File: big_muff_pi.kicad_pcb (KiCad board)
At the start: 2 copper layers, 56.3 x 18 mm, 54 parts, among them Q1 BC817, Q2 BC817, Q3 BC817, Q5 BC817

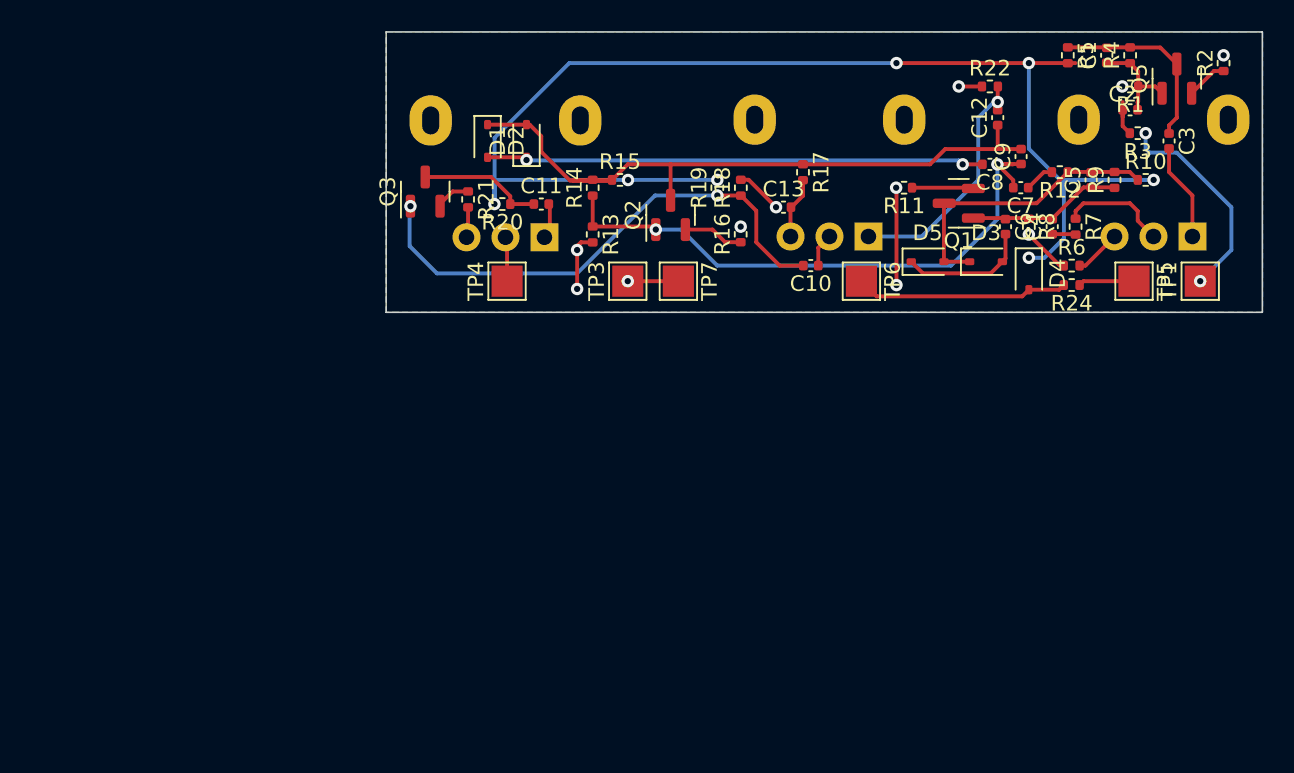
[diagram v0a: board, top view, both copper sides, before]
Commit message: Moved to 0603, all basic parts. Placement done.
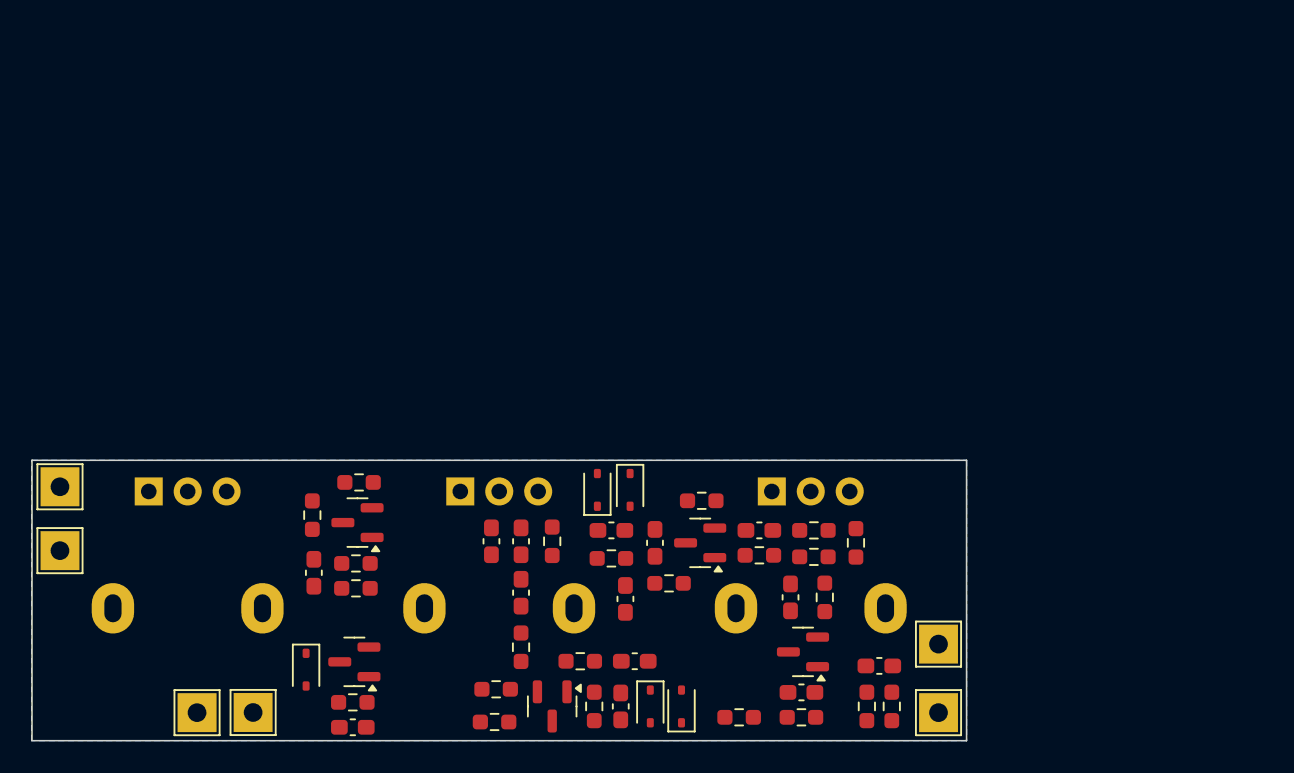
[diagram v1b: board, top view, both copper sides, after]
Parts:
- removed TP3: gnd, TestPoint:TestPoint_Pad_2.0x2.0mm
- removed TP5: Red Error LED, TestPoint:TestPoint_Pad_2.0x2.0mm
- removed TP6: Power Supply, TestPoint:TestPoint_Pad_2.0x2.0mm
- removed TP7: ground, TestPoint:TestPoint_Pad_2.0x2.0mm
- added C14: 10u, Capacitor_SMD:C_0603_1608Metric_Pad1.08x0.95mm_HandSolder, F.Cu at (120.6, 117.1)
- added Q4: MMBT5551, Package_TO_SOT_SMD:SOT-23, F.Cu at (149.5, 112.3)
- added TP11: input, TestPoint:TestPoint_THTPad_2.5x2.5mm_Drill1.2mm, F.Cu at (114.2, 116.2)
- added TP12: ground, TestPoint:TestPoint_THTPad_2.5x2.5mm_Drill1.2mm, F.Cu at (101.8, 105.8)
- added TP13: ground, TestPoint:TestPoint_THTPad_2.5x2.5mm_Drill1.2mm, F.Cu at (158.2, 111.8)
- added TP14: ground, TestPoint:TestPoint_THTPad_2.5x2.5mm_Drill1.2mm, F.Cu at (110.6, 116.2)
- C1, C10, C11, C13, C2, C3, C4, C5, C6, C7, C8, C9: footprint Capacitor_SMD:C_0402_1005Metric -> Capacitor_SMD:C_0603_1608Metric_Pad1.08x0.95mm_HandSolder
- C12: value 4n -> 4.7n; footprint Capacitor_SMD:C_0402_1005Metric -> Capacitor_SMD:C_0603_1608Metric_Pad1.08x0.95mm_HandSolder
- Q1, Q2, Q3, Q5: value BC817 -> MMBT5551
- R1, R10, R11, R12, R13, R14, R15, R16, R17, R18, R19, R2, R20, R21, R22, R3, R4, R5, R6, R7, R8, R9: footprint Resistor_SMD:R_0402_1005Metric -> Resistor_SMD:R_0603_1608Metric_Pad0.98x0.95mm_HandSolder
- R24: value 510 -> 1k; footprint Resistor_SMD:R_0402_1005Metric -> Resistor_SMD:R_0603_1608Metric_Pad0.98x0.95mm_HandSolder
- RV1: value 10k -> 100k
- TP1, TP4: footprint TestPoint:TestPoint_Pad_2.0x2.0mm -> TestPoint:TestPoint_THTPad_2.5x2.5mm_Drill1.2mm
- moved Q5 64.7 mm to (120.7, 112.9), turned to 180 degrees
- moved R24 53.4 mm to (120.6, 115.5)
- moved D4 52.9 mm to (117.6, 113.4)
- moved R4 47.4 mm to (149.4, 116.5), turned to 180 degrees
- moved R5 47.4 mm to (145.4, 116.5), turned to 0 degrees
- moved R22 46.9 mm to (131.4, 112.0), turned to 90 degrees
- moved C1 45.4 mm to (149.4, 114.9), turned to 180 degrees
- moved C9 43.7 mm to (137.8, 115.8), turned to -90 degrees
- moved R1 43.2 mm to (153.6, 115.8), turned to -90 degrees
- moved C12 43.2 mm to (131.4, 108.5), turned to -90 degrees
- moved R2 42.8 mm to (150.9, 108.8), turned to -90 degrees
- moved R3 40.0 mm to (155.2, 115.8), turned to 90 degrees
- moved C8 39.2 mm to (138.7, 112.9), turned to 0 degrees
- moved C2 39.2 mm to (154.4, 113.2), turned to 180 degrees
- moved D2 38.4 mm to (141.7, 115.8), turned to 90 degrees
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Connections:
- C1 pad 1: Net-(Q5-B) -> Net-(Q4-B)
- C1 pad 2: Net-(Q5-C) -> Net-(Q4-C)
- C2 pad 2: Net-(Q5-B) -> Net-(Q4-B)
- C3 pad 1: Net-(Q5-C) -> Net-(Q4-C)
- D4 pad 1: 9V -> Net-(D4-K)
- Q5 pad 2: Net-(Q5-E) -> 9V
- Q5 pad 3: Net-(Q5-C) -> Net-(D4-K)
- R1 pad 1: Net-(Q5-B) -> Net-(Q4-B)
- R10 pad 1: Net-(D3-K) -> 9V
- R10 pad 2: 9V -> Net-(D3-K)
- R15 pad 1: Net-(D1-A) -> 9V
- R15 pad 2: 9V -> Net-(D1-A)
- R2 pad 1: Net-(Q5-E) -> 0
- R2 pad 2: 0 -> Net-(Q4-E)
- R24 pad 1: Net-(R24-Pad1) -> Net-(Q5-B)
- R24 pad 2: Net-(D4-A) -> Net-(D4-K)
- R4 pad 1: Net-(Q5-B) -> Net-(Q4-B)
- R4 pad 2: Net-(Q5-C) -> Net-(Q4-C)
- R5 pad 1: Net-(Q5-C) -> 9V
- R5 pad 2: 9V -> Net-(Q4-C)
- R6 pad 1: 0 -> Net-(R6-Pad1)
- R6 pad 2: Net-(R6-Pad2) -> 0
- RV1 pad 3: Net-(R6-Pad2) -> Net-(R6-Pad1)
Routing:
- net 9V: track 86.0 -> 0.00 mm, vias 7 -> 0
- net Net-(D1-A): track 43.8 -> 0.00 mm
- net Net-(Q2-B): track 38.2 -> 0.00 mm, vias 2 -> 0
- net Net-(Q3-B): track 33.7 -> 0.00 mm, vias 2 -> 0
- net Net-(D1-K): track 32.0 -> 0.00 mm, vias 2 -> 0
- net 0: track 23.0 -> 0.00 mm, vias 11 -> 0
- net Net-(D3-K): track 18.9 -> 0.00 mm
- net Net-(C12-Pad2): track 15.7 -> 0.00 mm, vias 1 -> 0
- net Net-(D4-A): track 13.7 -> 0.00 mm
- net Net-(R3-Pad1): track 13.6 -> 0.00 mm, vias 2 -> 0
- net Net-(Q5-C): track 12.1 -> 0.00 mm
- net Net-(Q1-B): track 9.89 -> 0.00 mm
- net Net-(D3-A): track 8.32 -> 0.00 mm
- net Net-(Q3-C): track 7.98 -> 0.00 mm
- net Net-(R7-Pad1): track 6.95 -> 0.00 mm
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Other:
- board size 56.3 x 18 mm -> 60 x 18 mm

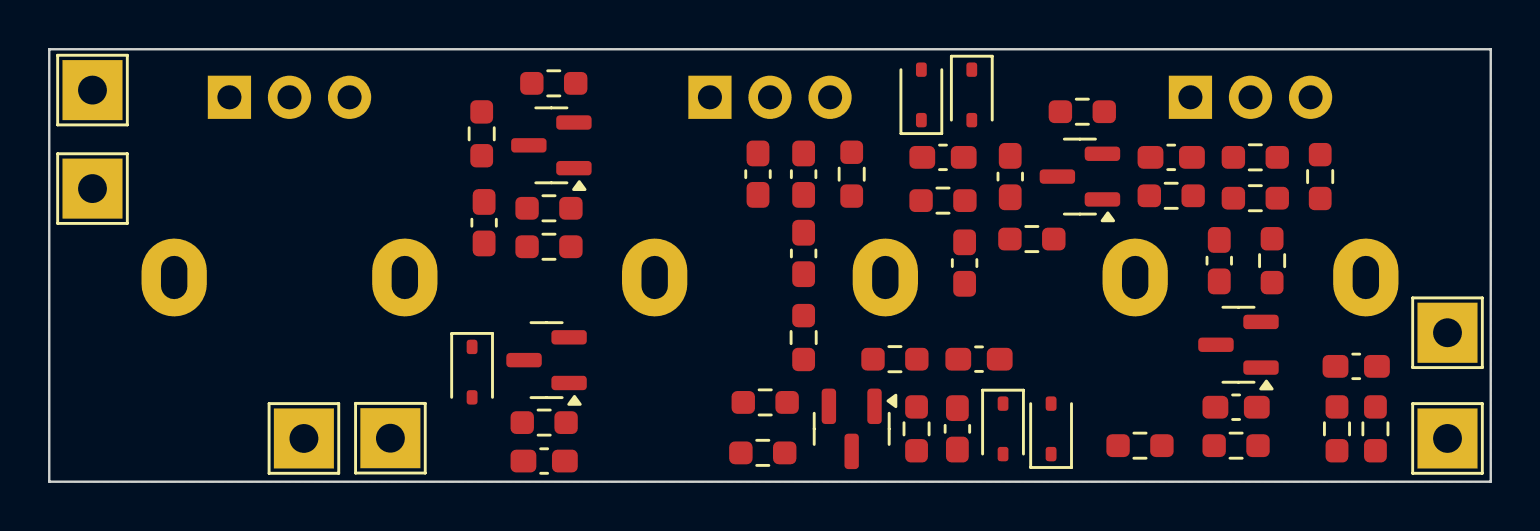
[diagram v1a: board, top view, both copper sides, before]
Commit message: Added capacitance, switches.
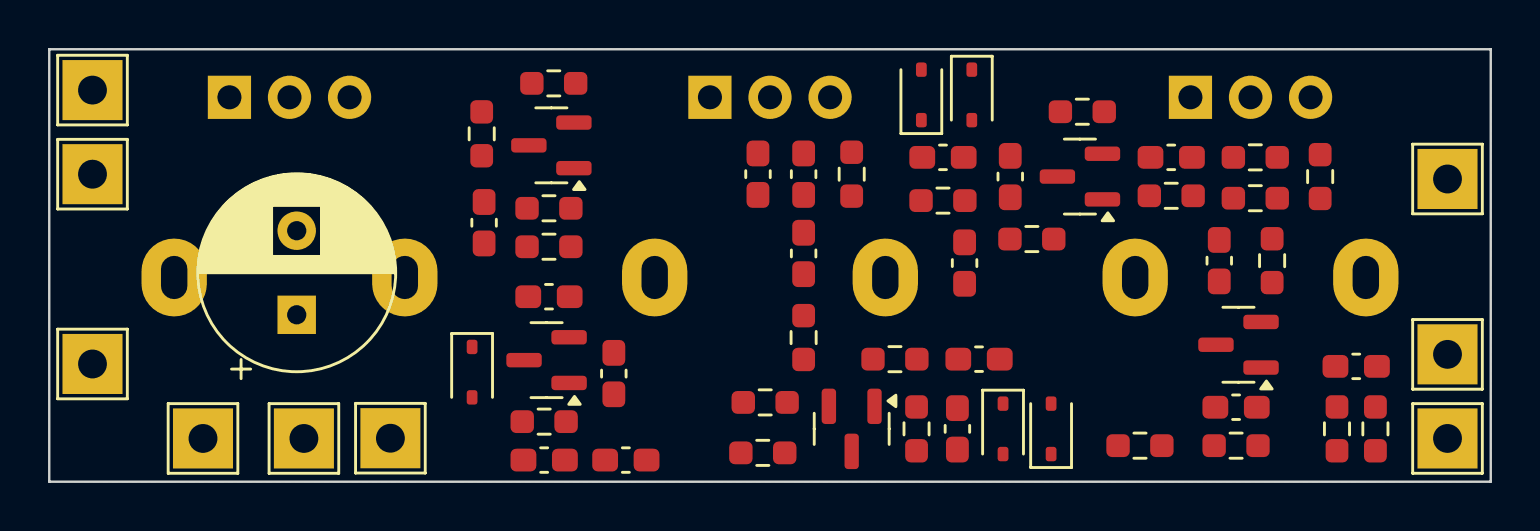
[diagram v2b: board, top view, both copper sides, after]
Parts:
- added C16: 10u, Capacitor_SMD:C_0603_1608Metric_Pad1.08x0.95mm_HandSolder, F.Cu at (120.8, 110.3)
- added C17: 10u, Capacitor_SMD:C_0603_1608Metric_Pad1.08x0.95mm_HandSolder, F.Cu at (123.5, 113.5)
- added C18: 100n, Capacitor_SMD:C_0603_1608Metric_Pad1.08x0.95mm_HandSolder, F.Cu at (124.0, 117.1)
- added C19: 470u, Capacitor_THT:CP_Radial_D8.0mm_P3.50mm, F.Cu at (110.3, 111.1)
- added TP15: SW_OFF, TestPoint:TestPoint_THTPad_2.5x2.5mm_Drill1.2mm, F.Cu at (158.2, 112.7)
- added TP16: SW_ON, TestPoint:TestPoint_THTPad_2.5x2.5mm_Drill1.2mm, F.Cu at (106.4, 116.2)
- added TP5: output, TestPoint:TestPoint_THTPad_2.5x2.5mm_Drill1.2mm, F.Cu at (101.8, 105.2)
- TP4: value output -> SW_MID
- moved TP12 7.30 mm to (101.8, 113.1)
- moved TP13 6.40 mm to (158.2, 105.4)
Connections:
- TP4 pad 1: Net-(RV3-Pad2) -> Net-(TP4-Pad1)

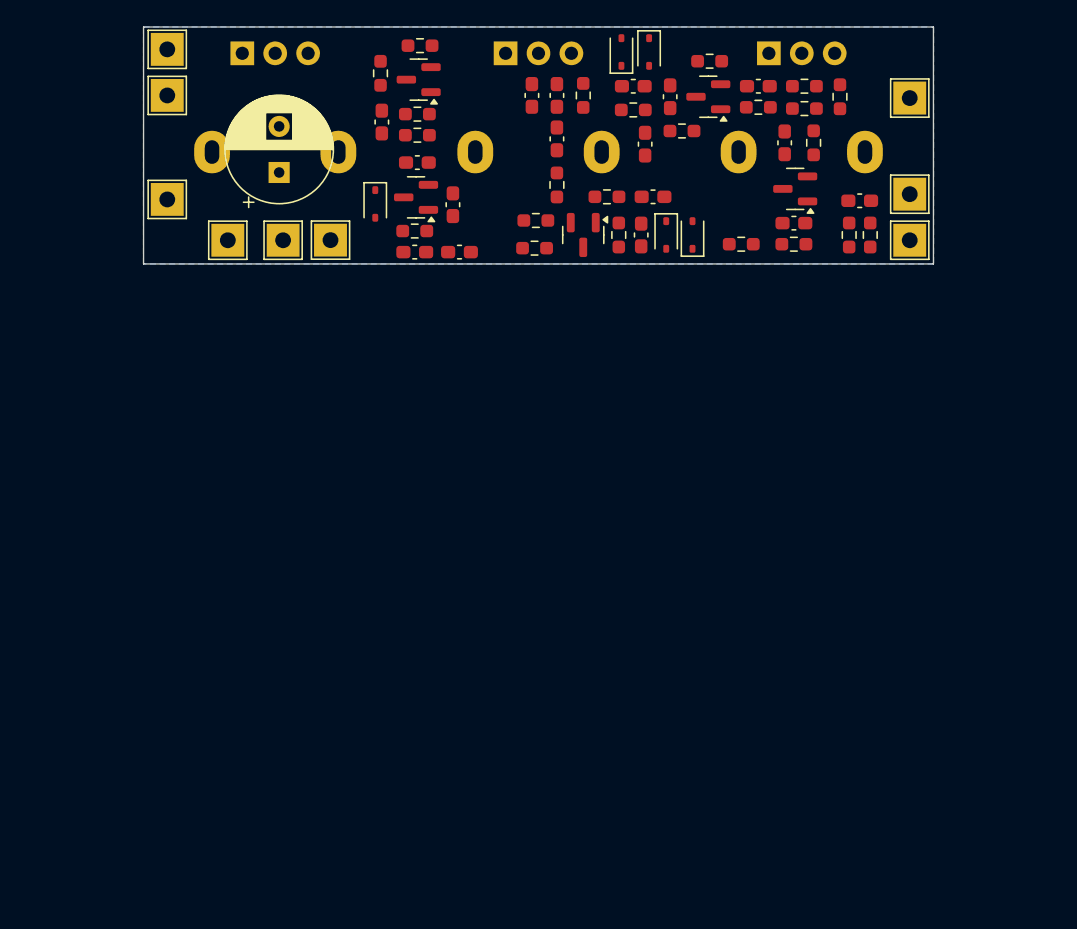
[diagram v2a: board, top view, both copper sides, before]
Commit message: Added connectors and switched.
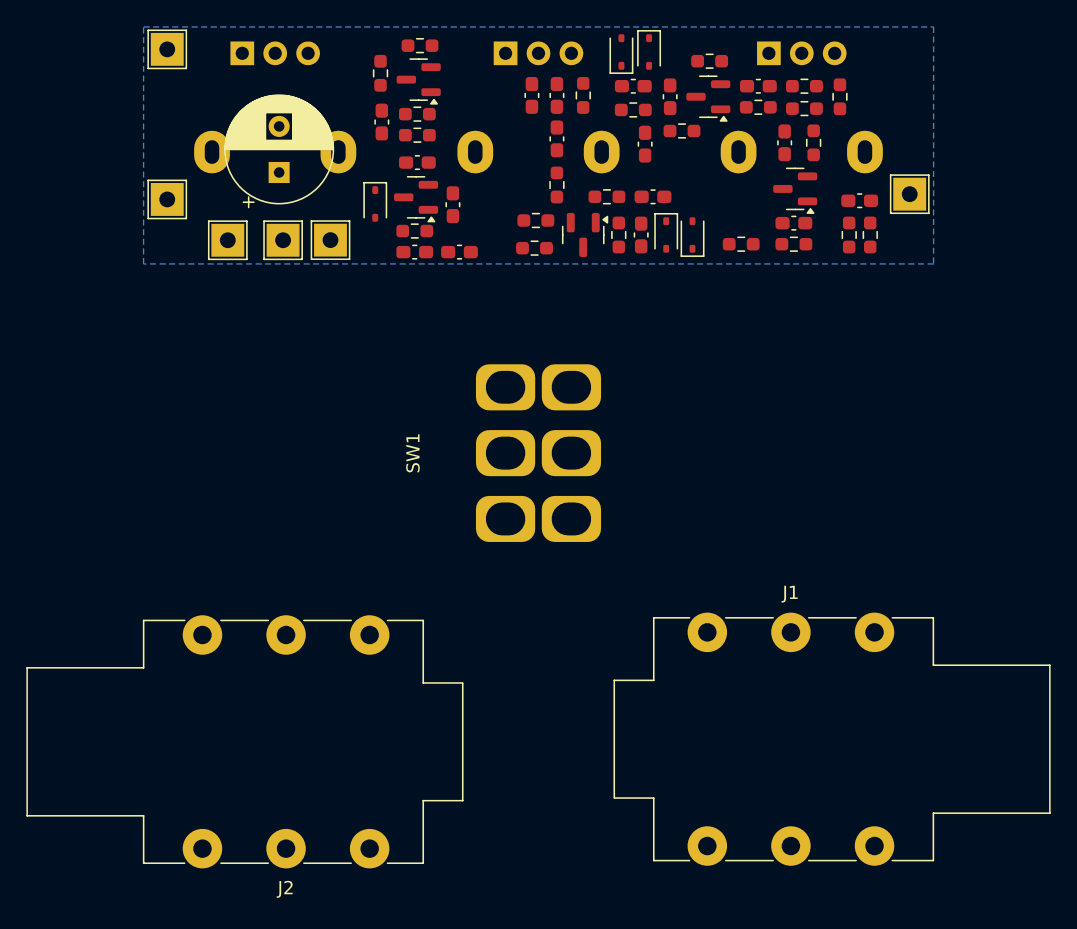
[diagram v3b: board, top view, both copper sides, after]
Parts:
- removed TP1: input, TestPoint:TestPoint_THTPad_2.5x2.5mm_Drill1.2mm
- removed TP13: ground, TestPoint:TestPoint_THTPad_2.5x2.5mm_Drill1.2mm
- removed TP5: output, TestPoint:TestPoint_THTPad_2.5x2.5mm_Drill1.2mm
- added J1: NMJ6HHD2, Connector_Audio:Jack_6.35mm_Neutrik_NMJ6HHD2_Horizontal, F.Cu at (142.8, 146.0)
- added J2: NMJ6HHD2, Connector_Audio:Jack_6.35mm_Neutrik_NMJ6HHD2_Horizontal, F.Cu at (117.2, 162.4)
- added SW1: SW_DPDT_x2, switch:switch_DPDT, F.Cu at (127.5, 137.4)
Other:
- board outline removed
